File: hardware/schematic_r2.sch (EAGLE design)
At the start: 39 parts, among them J1 SMA_EDGE, U1 HX1, U2 TPS62160, U3 LMC6482

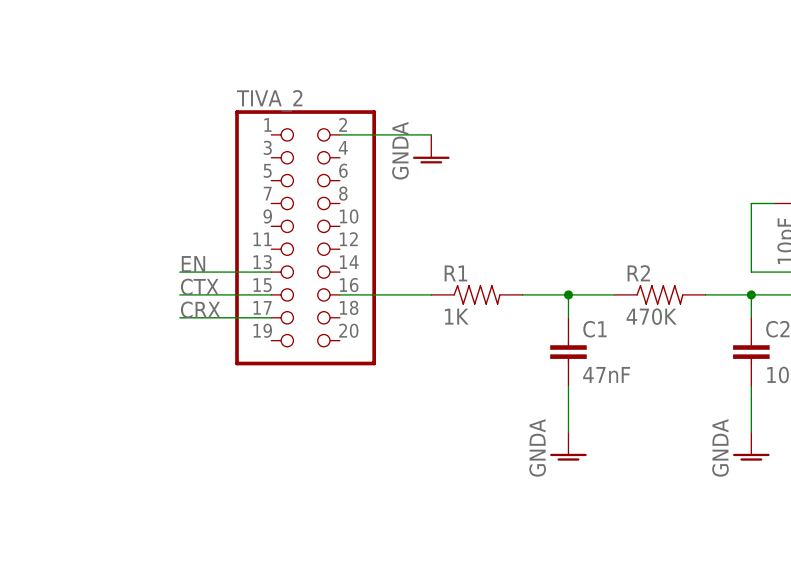
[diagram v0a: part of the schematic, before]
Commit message: fixed TX RX naming for copernicus (was swapped), fixed AX.25 PWM output port to correct one
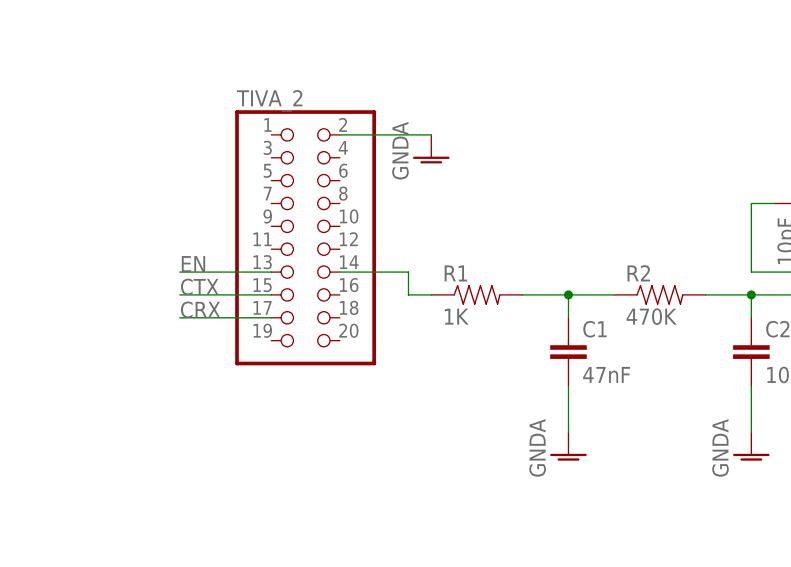
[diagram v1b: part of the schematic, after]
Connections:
- net PWMOUT: now also TIVA_2.14; no longer TIVA_2.16
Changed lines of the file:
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@@
 <net name="PWMOUT" class="0">
 <segment>
-<pinref part="TIVA_2" gate="A" pin="16"/>
 <pinref part="R1" gate="G$1" pin="1"/>
-<wire x1="7.62" y1="12.7" x2="17.78" y2="12.7" width="0.1524" layer="91"/>
+<wire x1="15.24" y1="12.7" x2="17.78" y2="12.7" width="0.1524" layer="91"/>
+<pinref part="TIVA_2" gate="A" pin="14"/>
+<wire x1="7.62" y1="15.24" x2="15.24" y2="15.24" width="0.1524" layer="91"/>
+<wire x1="15.24" y1="15.24" x2="15.24" y2="12.7" width="0.1524" layer="91"/>
 </segment>
 </net>

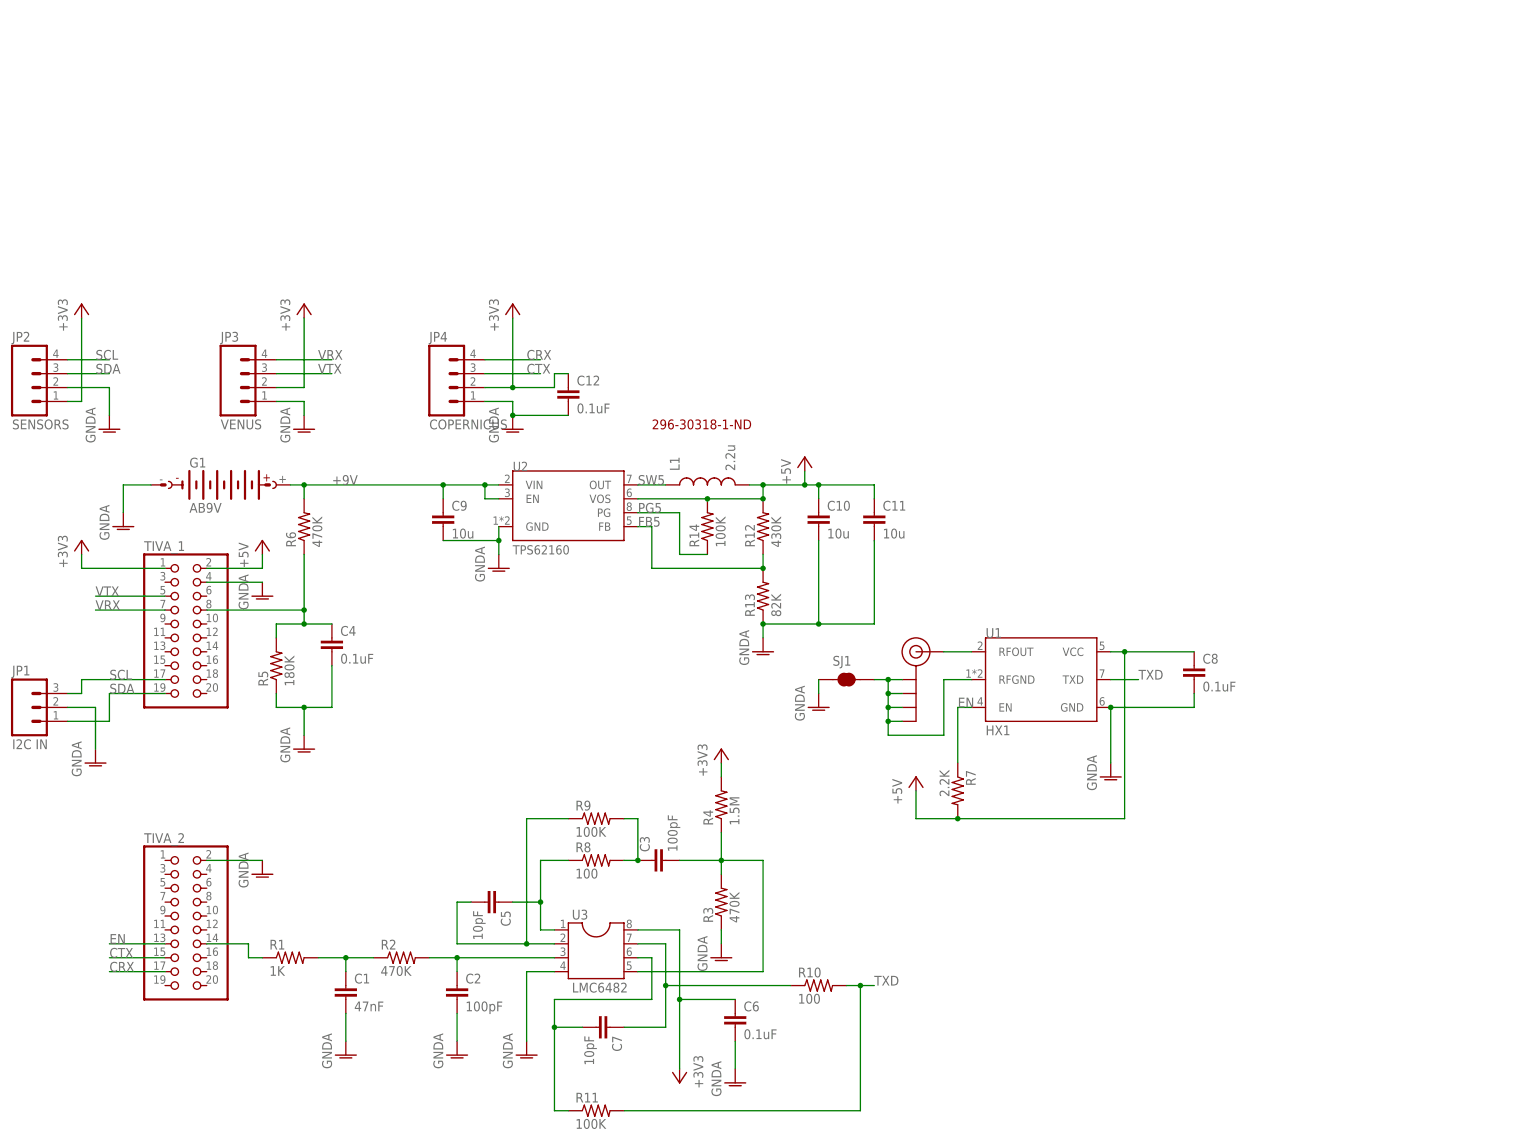
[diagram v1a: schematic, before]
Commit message: Fixed #26: fix PCB bugs in Revision 2 schematics and board
Note that subsequent flights should really use an STM32-based telemetry board to get better power usage and weight.
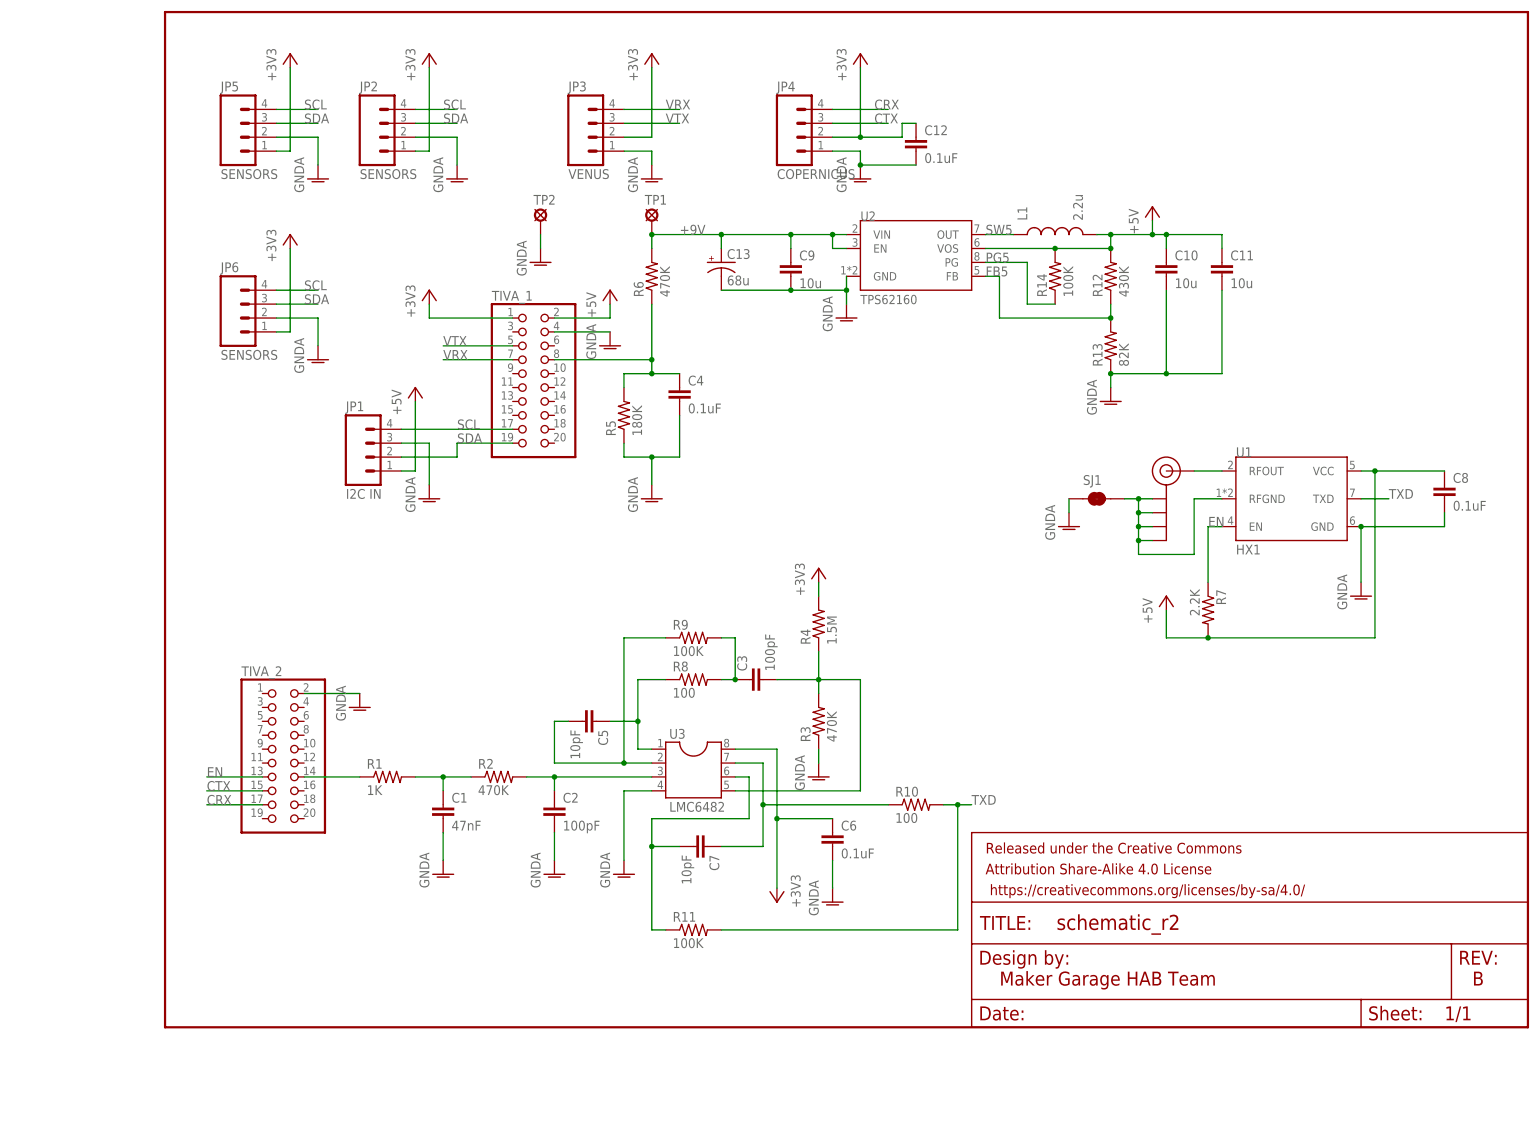
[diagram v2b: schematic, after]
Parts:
- removed G1: AB9V, battery:AB9V
- added C13: 68u, SparkFun-Passives:CAP_POLPTH2
- added FRAME1: FRAME-LETTERNO_PACKAGE, SparkFun-Aesthetics:FRAME-LETTERNO_PACKAGE
- added JP5, JP6: SENSORS, SparkFun-Connectors:M04PTH
- added TP1, TP2: MCS08, solpad:MCS08
- JP1: device SparkFun-Connectors:M03PTH -> SparkFun-Connectors:M04PTH
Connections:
- net +3V3: now also JP5.1, JP6.1
- net +5V: now also JP1.1
- net +9V: now also C13.+, TP1.MP; no longer G1.+
- net GNDA: now also C13.-, JP1.3, JP5.2, JP6.2, TP2.MP; no longer G1.-, JP1.2
- net SCL: now also JP1.4, JP5.4, JP6.4; no longer JP1.3
- net SDA: now also JP1.2, JP5.3, JP6.3; no longer JP1.1
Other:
- note added: "B"
- note added: "L1: CVH252009-2R2MCT-ND C9-C11: 490-5523-1-ND C13: P15139-ND"
- note added: "Maker Garage HAB Team"
- note removed: "296-30318-1-ND"
- moved on the sheet: C1, C10, C11, C12, C2, C3, C4, C5, C6, C7, C8, C9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

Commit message: Start work on second generation telemetry MCU board. Only 6 batteries, more reliable, smaller, and lighter!
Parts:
- L1: device HAB:INDUCTOR -> HAB:INDUCTOR1008
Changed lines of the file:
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@@
 <part name="C8" library="SparkFun-Passives" deviceset="CAP" device="0805" value="0.1uF"/>
 <part name="U2" library="HAB" deviceset="TPS62160" device=""/>
-<part name="L1" library="HAB" deviceset="INDUCTOR" device="" value="2.2u"/>
+<part name="L1" library="HAB" deviceset="INDUCTOR" device="1008" value="2.2u"/>
 <part name="P+2" library="supply1" deviceset="+5V" device=""/>
 <part name="GND12" library="supply1" deviceset="GNDA" device=""/>
